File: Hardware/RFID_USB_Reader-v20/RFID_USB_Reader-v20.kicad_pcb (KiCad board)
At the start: 2 copper layers, 44.5 x 31.8 mm, 47 parts, among them J1 USB_C_Receptacle, J3 SMD_1x1mm, J5 Conn_01x08, Q1 MMBT2222A, U3 CH340C

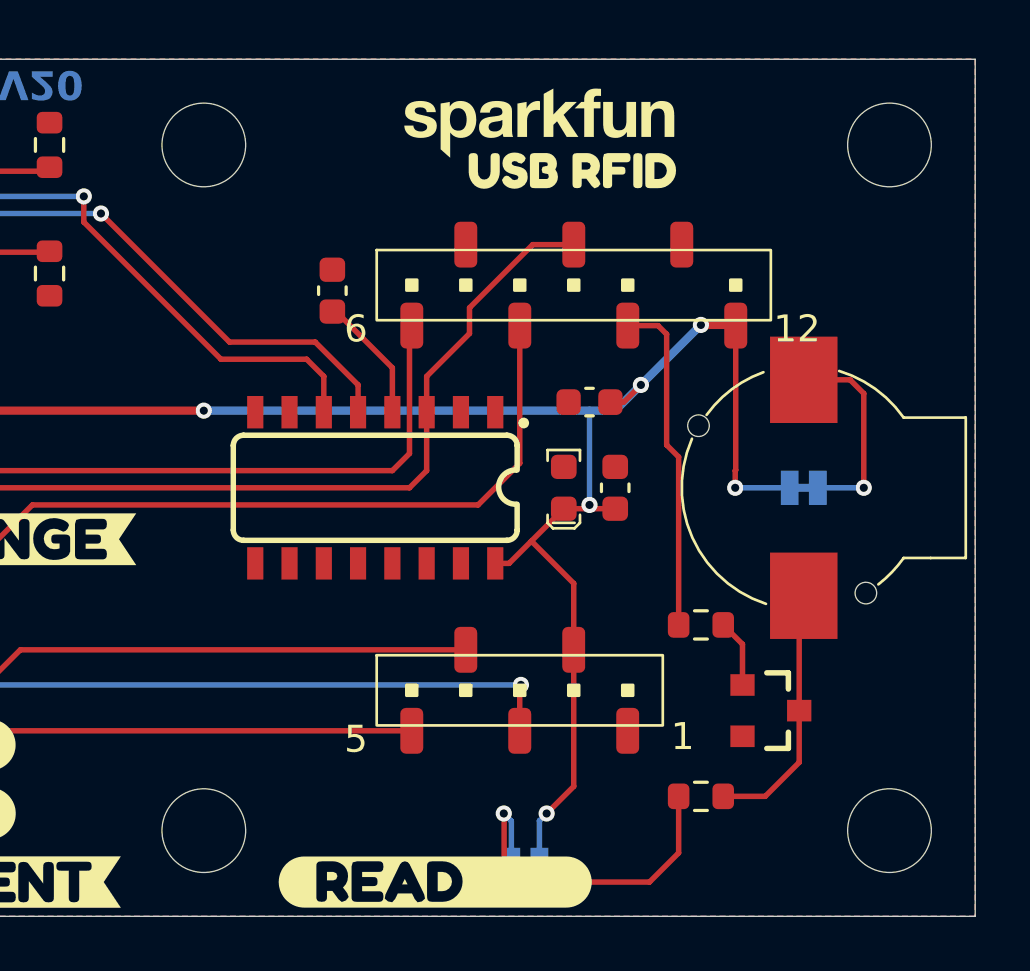
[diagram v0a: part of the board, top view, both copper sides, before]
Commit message: Update to small symbols. Add RFID outline device.
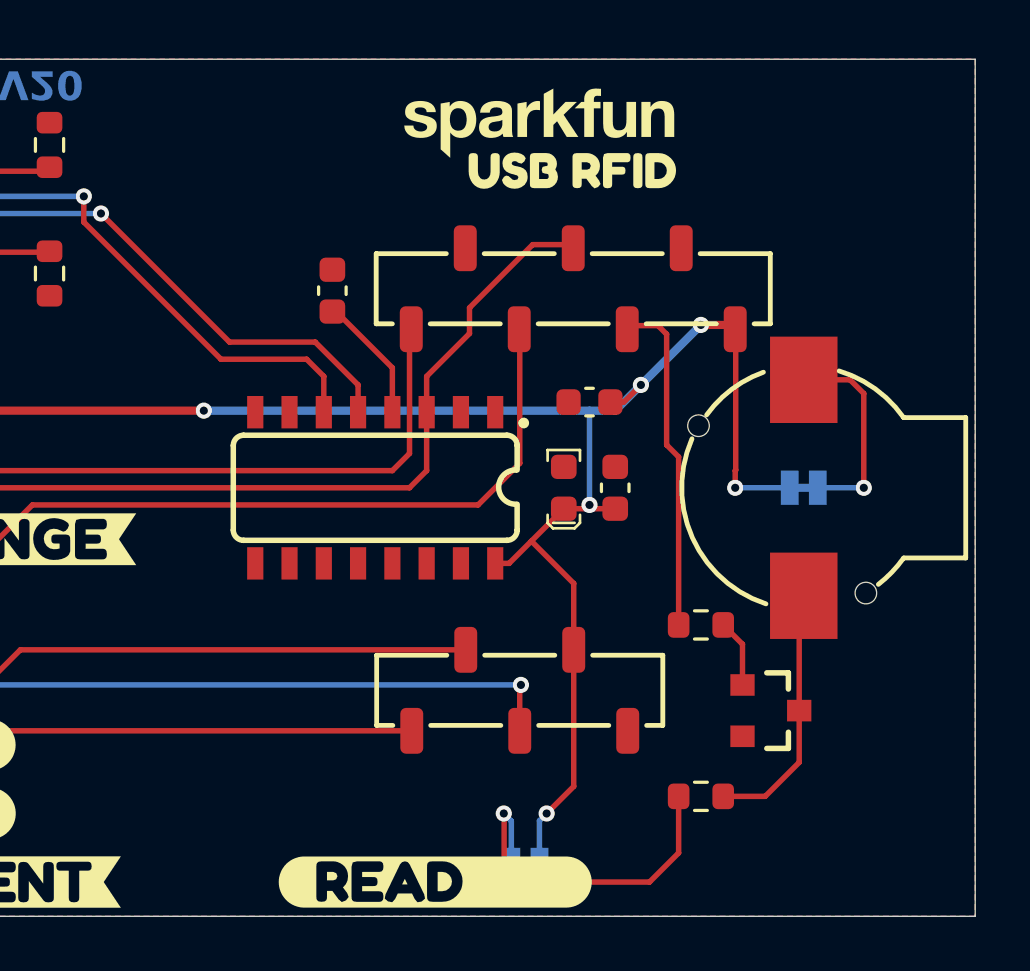
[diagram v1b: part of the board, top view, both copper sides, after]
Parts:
- removed J4: ~, SparkFun-Connector:1x07_SMD_2mm
- removed REF** (x4): Standoff, SparkFun-Hardware:Standoff
- removed REF**: ID-2/12/20-SMD, SparkFun-RF:ID-2_12_20-SMD
- removed U1: ~, SparkFun-Electromechanical:Buzzer_CCV
- added BZ1: Buzzer, SparkFun-Electromechanical:Buzzer_9mm_SMD, F.Cu at (219.1, 96.5)
- added J2: Conn_01x07_SMD_2.0mm, SparkFun-Connector:1x07_SMD_2mm_Pin1RightDown, F.Cu at (210.5, 89.1)
- added O1: RFID Outline, SparkFun-RF:ID-2_12_20_Outline, F.Cu at (209.6, 96.5)
- C4: value 10uF TANT -> 10uF
- J3: value SMD_1x1mm -> Conn_01x05_SMD_2.0mm; footprint SparkFun-Connector:1x05_SMD_2mm -> SparkFun-Connector:1x05_SMD_2mm_Pin1RightDown
- JP1: value ~ -> BUZZ
- JP2: value ~ -> LED
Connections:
- C4 pad 1: GND -> VCC
- C4 pad 2: VCC -> GND
- Q1 pad 3: Net-(Q1-C) -> Net-(BZ1--)
- R1 pad 1: Net-(J1-CC1) -> GND
- R1 pad 2: GND -> Net-(J1-CC1)
- R2 pad 1: Net-(J1-CC2) -> GND
- R2 pad 2: GND -> Net-(J1-CC2)
- R3 pad 1: Net-(D1-K) -> Net-(BZ1--)
- R3 pad 2: Net-(Q1-C) -> Net-(D1-K)
- R4 pad 1: Net-(Q1-B) -> LED
- R4 pad 2: LED -> Net-(Q1-B)
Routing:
- net Net-(Q1-B): track 2.52 -> 15.0 mm
- net LED: track 12.5 -> 0.00 mm
- net Net-(Q1-C): track 9.58 -> 0.00 mm
- net (no net): track 0.00 -> 9.58 mm

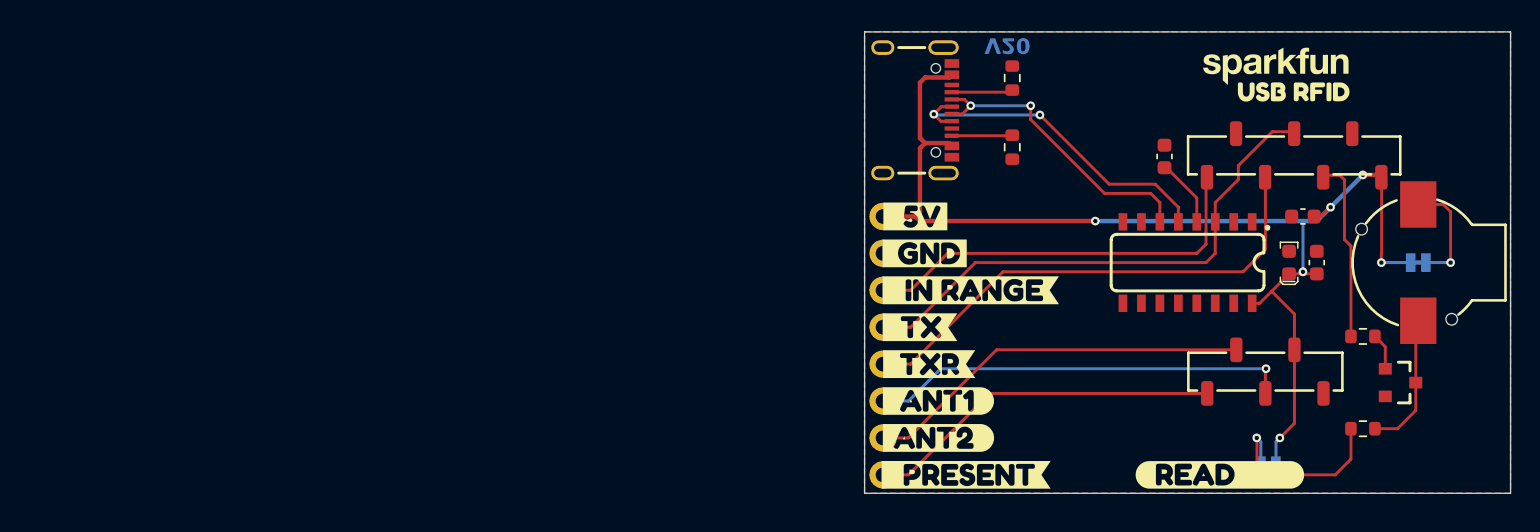
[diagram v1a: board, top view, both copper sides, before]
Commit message: Add fiducials. Add logos. Letter size.
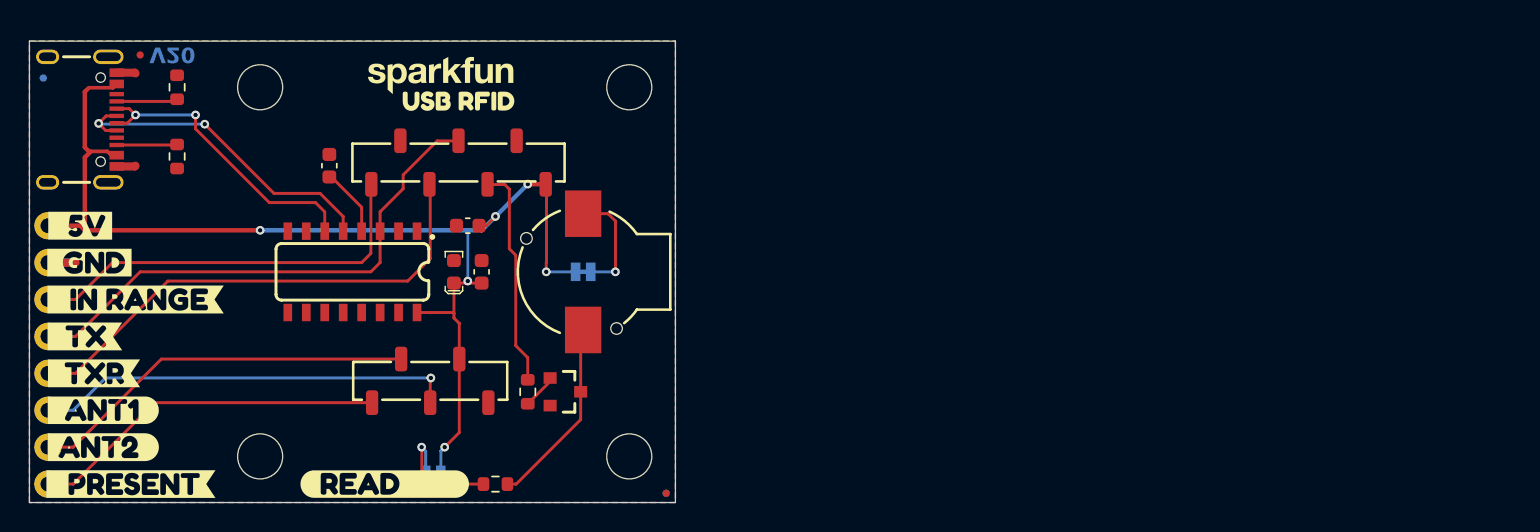
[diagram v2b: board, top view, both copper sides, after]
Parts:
- added FID1: Fiducial_0.5mm, SparkFun-Aesthetic:Fiducial_0.5mm_Mask1mm, B.Cu at (167.3, 112.4)
- added FID2: Fiducial_0.5mm, SparkFun-Aesthetic:Fiducial_0.5mm_Mask1mm, F.Cu at (131.1, 82.2)
- added FID3: Fiducial_0.5mm, SparkFun-Aesthetic:Fiducial_0.5mm_Mask1mm, B.Cu at (124.5, 83.8)
- added FID4: Fiducial_0.5mm, SparkFun-Aesthetic:Fiducial_0.5mm_Mask1mm, F.Cu at (167.3, 112.4)
- added G2: OSHW_Logo, SparkFun-Aesthetic:Creative_Commons_License, F.Cu at (236.0, 162.9)
- added ST1: Standoff, SparkFun-Hardware:Standoff, F.Cu at (164.8, 109.9)
- added ST2: Standoff, SparkFun-Hardware:Standoff, F.Cu at (164.8, 84.5)
- added ST3: Standoff, SparkFun-Hardware:Standoff, F.Cu at (139.4, 84.5)
- added ST4: Standoff, SparkFun-Hardware:Standoff, F.Cu at (139.4, 109.9)
- moved R3 59.8 mm to (155.6, 111.8), turned to 180 degrees
- moved R4 57.6 mm to (157.8, 105.4), turned to -90 degrees
- moved J2 57.5 mm to (153.0, 89.6)
- moved Ref** 57.5 mm to (126.4, 86.7)
- moved BZ1 57.5 mm to (161.6, 97.2)
- moved C1 57.5 mm to (144.1, 89.9)
- moved C2 57.5 mm to (153.7, 94.0)
- moved C3 57.5 mm to (154.6, 97.2)
- moved C4 57.5 mm to (152.7, 97.2), turned to 90 degrees
- moved D1 57.5 mm to (151.3, 111.8)
- moved G*** 57.5 mm to (151.8, 83.5)
- moved G*** 57.5 mm to (147.0, 95.2)
- moved J1 57.5 mm to (129.9, 86.7)
- moved J3 57.5 mm to (151.1, 104.7)
- moved J5 57.5 mm to (124.8, 111.8)
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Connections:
- net VCC renamed 5V
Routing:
- net LED: track 0.00 -> 15.2 mm
- net Net-(BZ1--): track 0.00 -> 13.1 mm
- net Net-(Q1-B): track 15.0 -> 2.41 mm
- net (no net): track 9.58 -> 0.00 mm
- net GND: track 0.00 -> 6.13 mm
- net Net-(D1-K): track 7.43 -> 2.67 mm
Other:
- copper layers 2 -> 4
- rule pad_to_mask_clearance: 0 -> 0.05

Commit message: Add 3D models
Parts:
- removed kibuzzard-677EEEC6: G***, kibuzzard-677EEEC6
- added kibuzzard-67819308: G***, kibuzzard-67819308, B.Cu at (161.6, 94.9)
- J2: value Conn_01x07_SMD_2.0mm -> Conn_01x07_2.0mm; footprint SparkFun-Connector:1x07_SMD_2mm_Pin1RightDown -> SparkFun-Connector:1x07_2.0mm_SMD_Pin1RightDown
- J3: value Conn_01x05_SMD_2.0mm -> Conn_01x05_2.0mm; footprint SparkFun-Connector:1x05_SMD_2mm_Pin1RightDown -> SparkFun-Connector:1x05_2.0mm_SMD_Pin1RightDown
